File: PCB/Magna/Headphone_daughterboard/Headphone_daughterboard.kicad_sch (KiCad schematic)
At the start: 47 parts, among them J101 Conn_02x05_Odd_Even, J102 AudioJack3, U101 NE5532, U102 NE5532, U103 TDA2822D

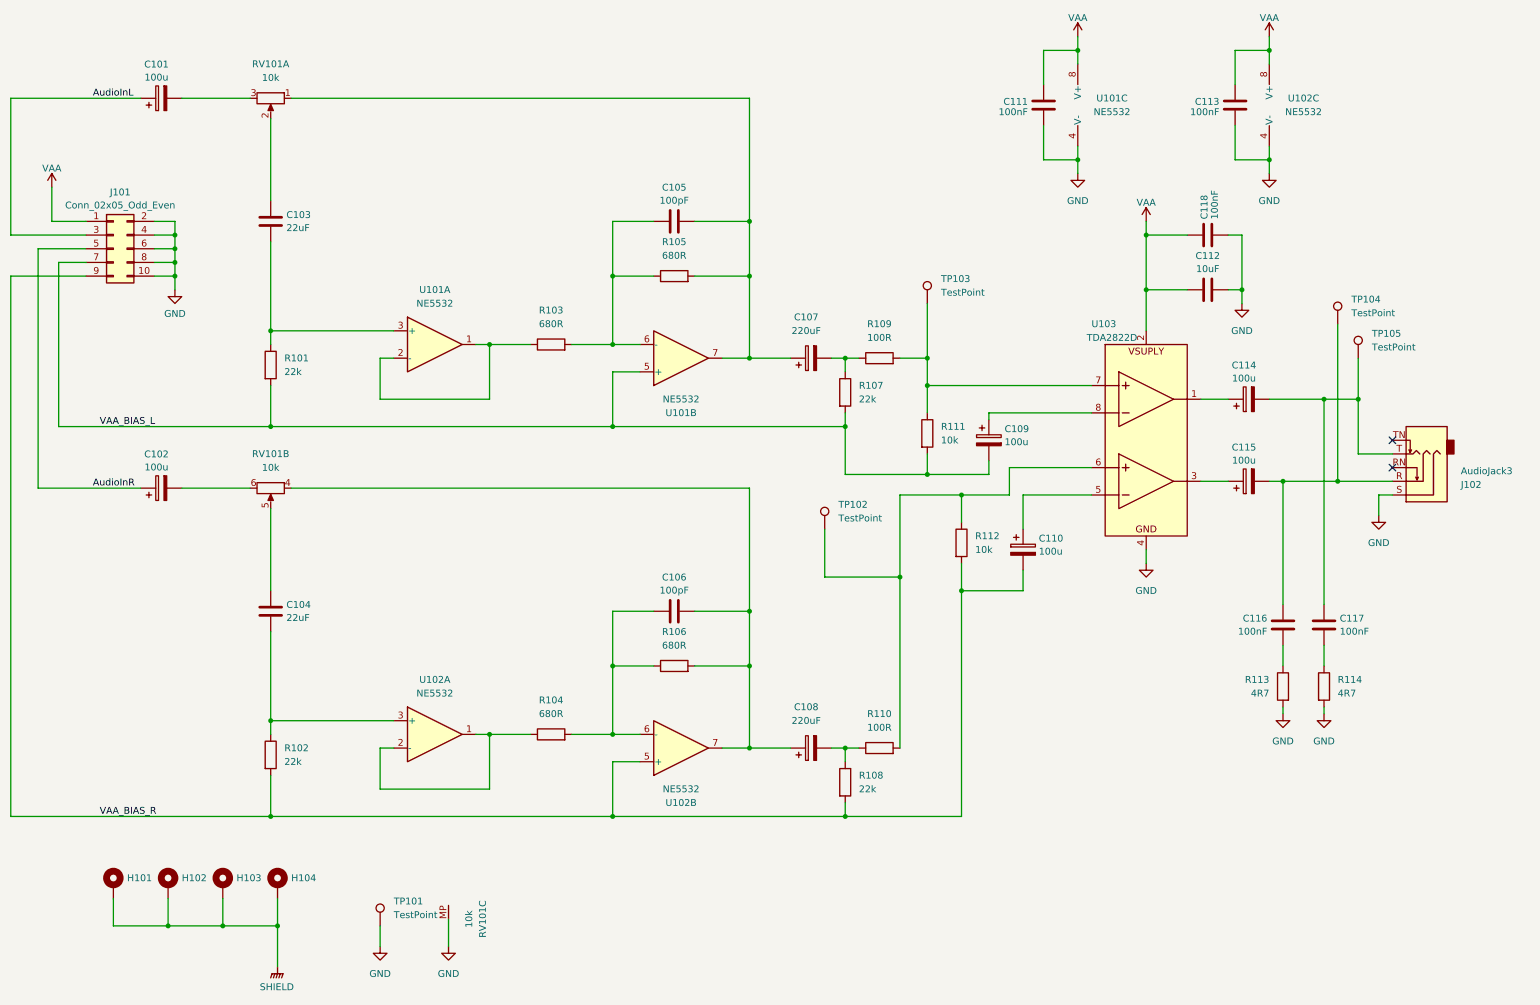
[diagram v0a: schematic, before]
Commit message: Fix board alignments and mounting holes
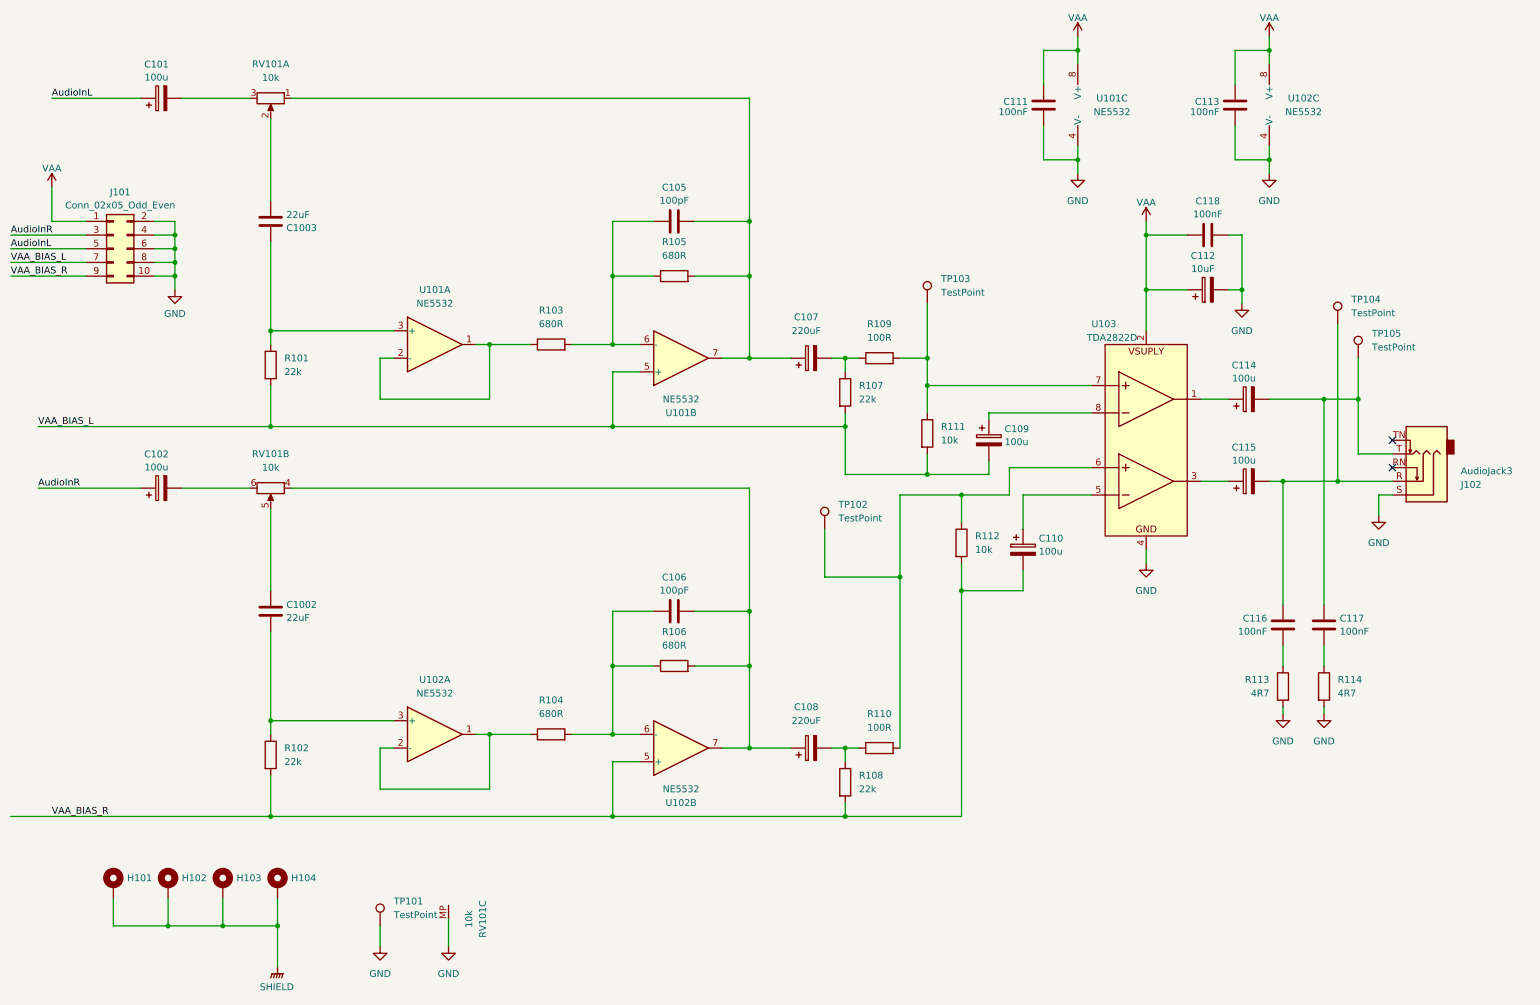
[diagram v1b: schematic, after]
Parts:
- removed C103, C104: 22uF, Skrooter_footprints:c_elec_SMD_12.5x13.5, symbol Device:C
- added C1002, C1003: 22uF, Capacitor_SMD:CP_Elec_6.3x5.4, symbol Device:C
- C112: symbol Device:C -> Device:C_Polarized; now in the parts list
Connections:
- net AudioInL: now also J101.5 (Pin_5); no longer J101.3 (Pin_3)
- net AudioInR: now also J101.3 (Pin_3); no longer J101.5 (Pin_5)
- net at RV101.5: now also C1002.1
- net at R101.1, U101.3 (+): now also C1003.2
- net at RV101.2: now also C1003.1
- net at R102.1, U102.3 (+): now also C1002.2
